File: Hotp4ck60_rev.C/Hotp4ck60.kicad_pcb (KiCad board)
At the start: 2 copper layers, 284.7 x 94.2 mm, 171 parts, among them J1 Conn_01x05_Pin, J2 Conn_01x05_Socket, J3 TC2030_SWD, SW1 SW_DIP_x01, U1 nRF52840_E73-2G4M08S1C, U2 BQ24075, U3 MAX17048, Y1 32.768 KHz

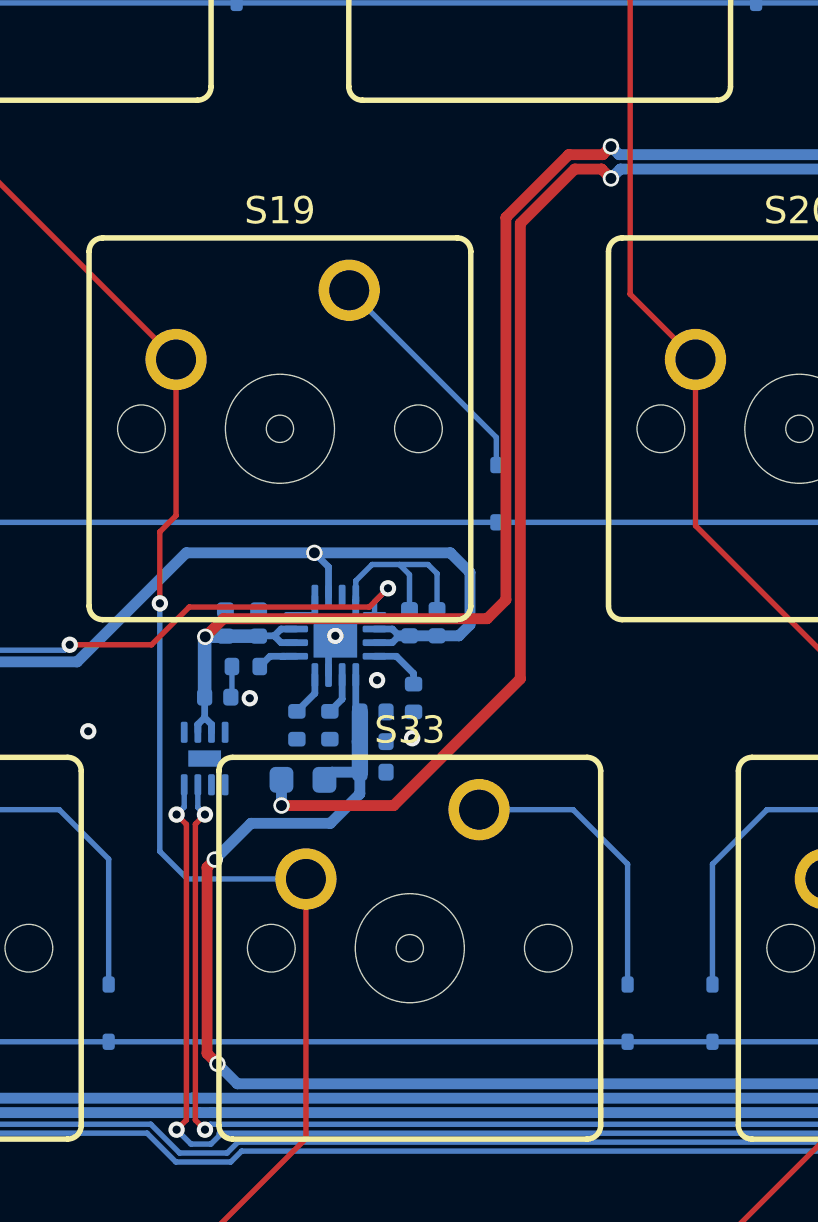
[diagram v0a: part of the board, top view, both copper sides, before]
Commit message: 전우너 관리 IC 타이머 저항 수정
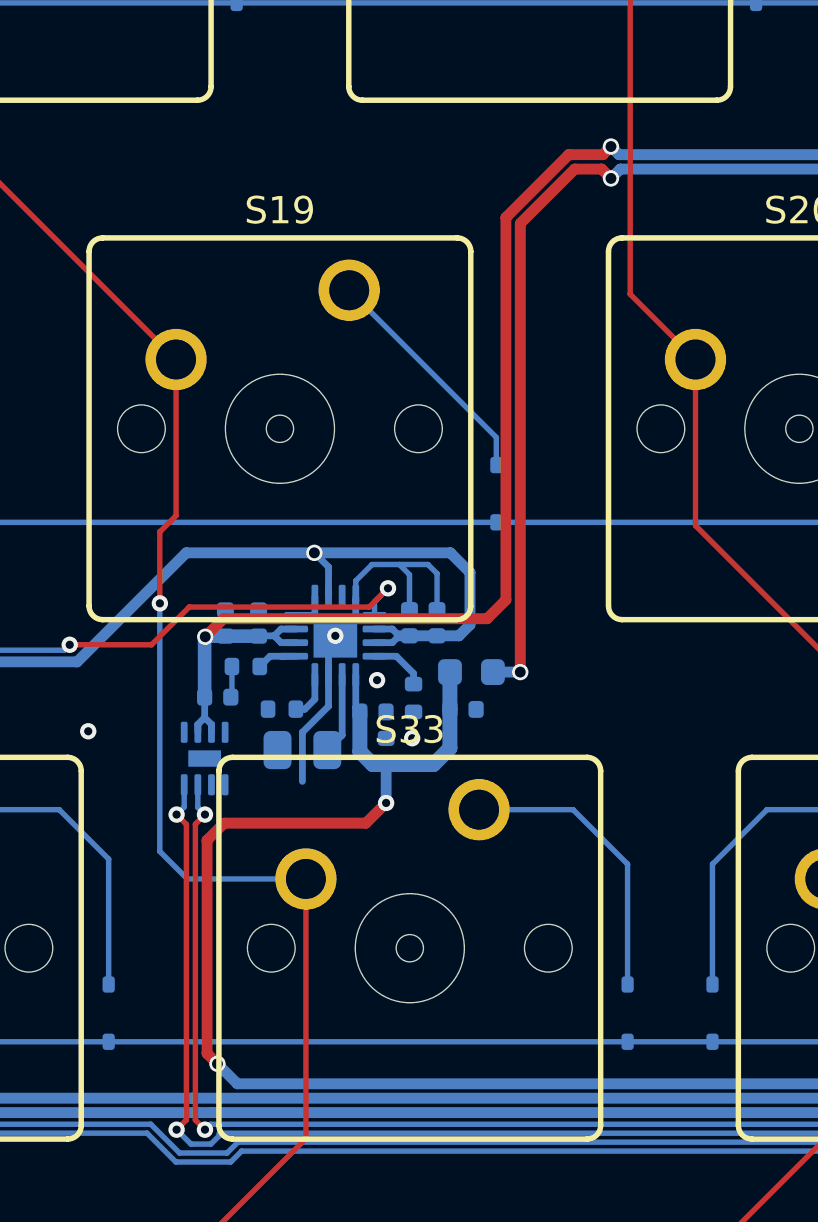
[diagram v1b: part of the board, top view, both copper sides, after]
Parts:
- R4: value 15k -> 68k; footprint Resistor_SMD:R_0402_1005Metric -> Resistor_SMD:R_0805_2012Metric
- R6: value 910 -> 2k2
- moved F1 7.34 mm to (133.2, 61.3), turned to 0 degrees
- moved C1 4.03 mm to (132.9, 62.7)
- moved R4 1.36 mm to (127.0, 64.2), turned to 180 degrees
- moved R6 0.81 mm to (126.3, 62.7), turned to 180 degrees
- moved C2 0.60 mm to (130.1, 64.2), turned to 90 degrees
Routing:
- net VBUS: track 63.2 -> 52.3 mm
- net +5V: track 110.6 -> 117.0 mm
- net GND: track 21.0 -> 25.3 mm, vias 36 -> 35
- net /TMR: track 1.52 -> 2.98 mm
